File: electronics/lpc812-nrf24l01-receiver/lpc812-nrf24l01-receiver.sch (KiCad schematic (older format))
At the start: 10 parts, among them K1 CONN_3, K2 CONN_3, K3 CONN_3, K4 CONN_3, P1 CONN_4X2, U1 MCP1703T-3302E/CB, U2 LPC812M101JDH16_TSSOP16

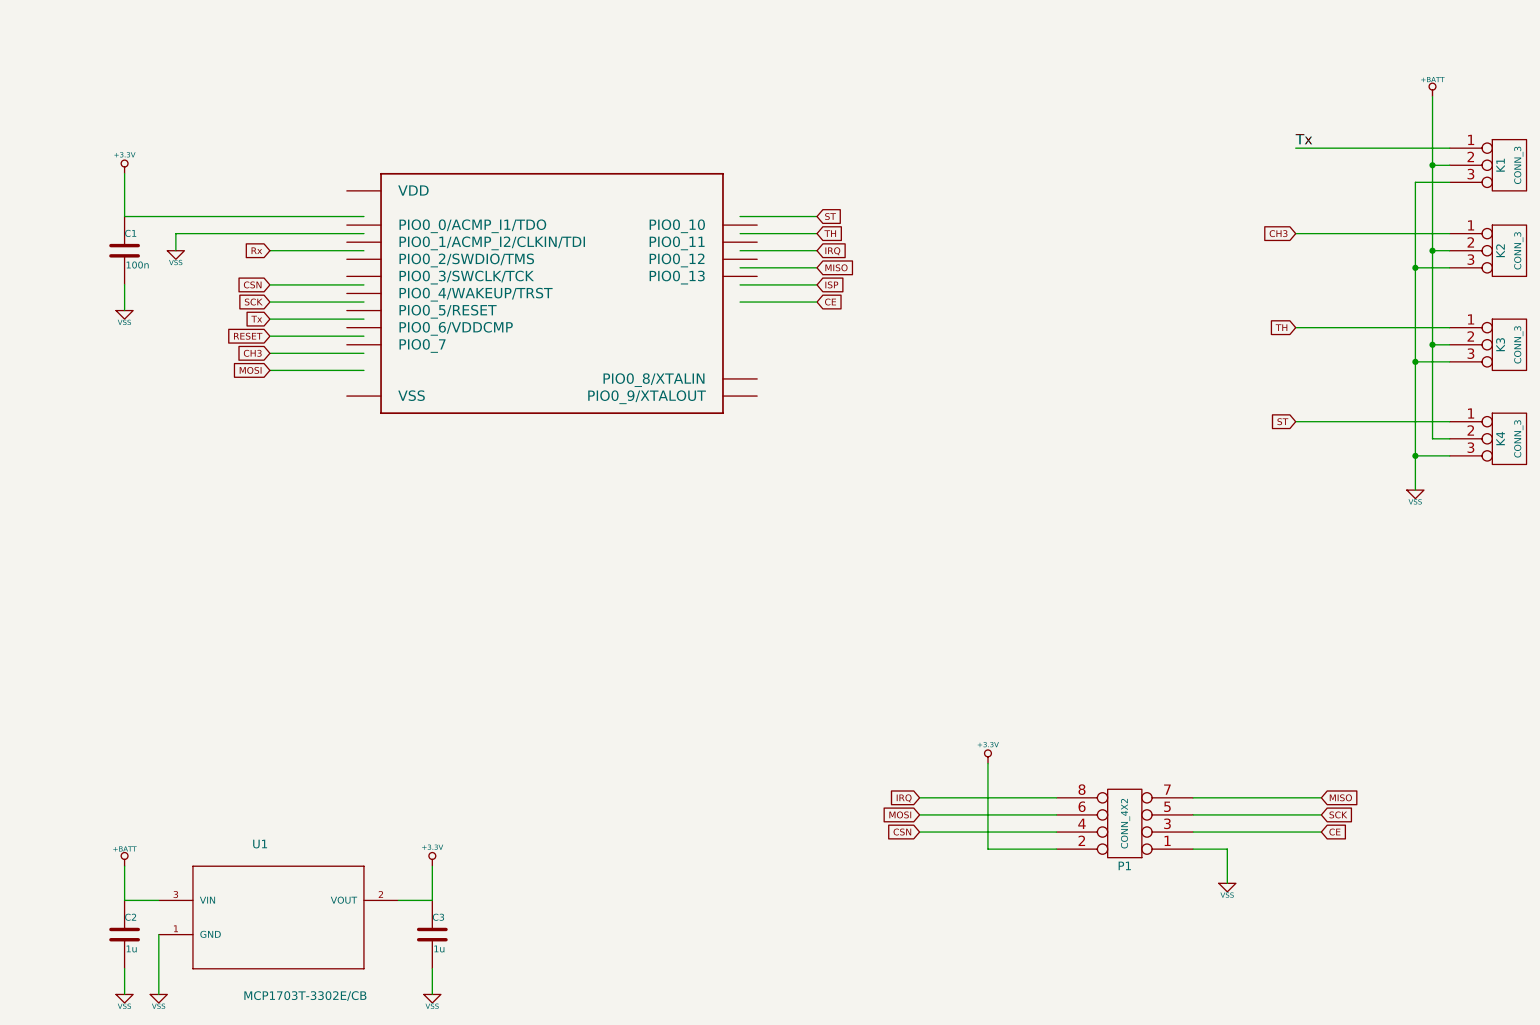
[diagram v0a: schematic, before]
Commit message: More tweaks to schematics and LPC812 symbol
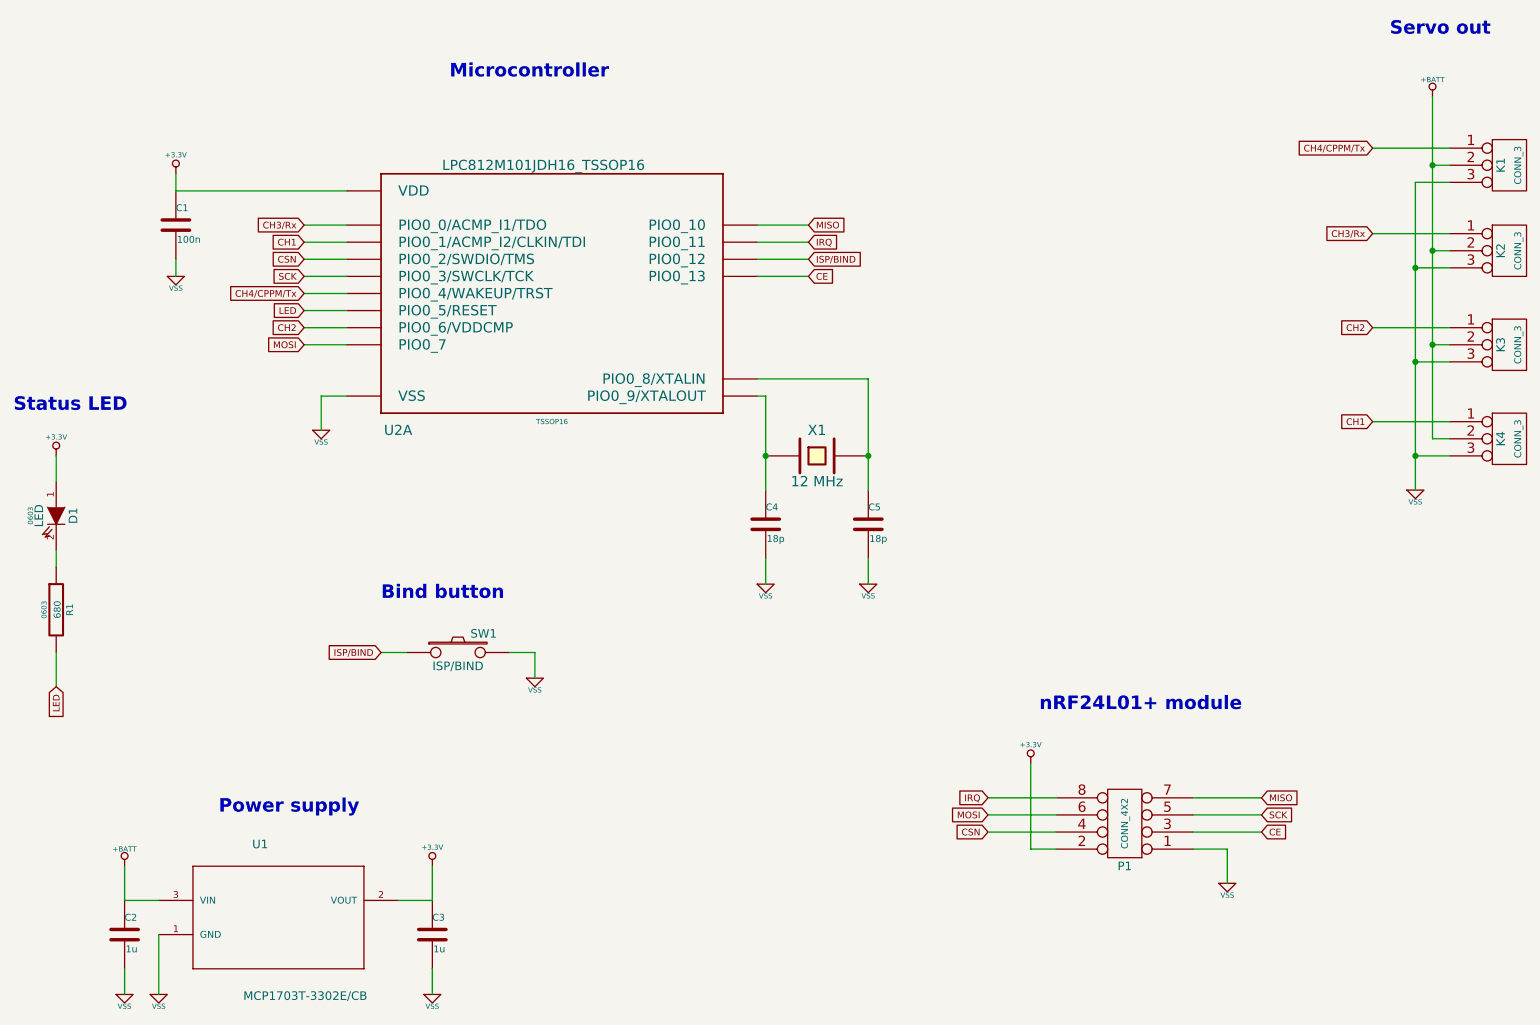
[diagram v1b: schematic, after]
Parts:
- added C4, C5: 18p, ~, symbol C
- added D1: LED, 0603, symbol LED
- added R1: 680, 0603, symbol R
- added SW1: ISP/BIND, ~, symbol SW_PUSH
- added X1: 12 MHz, ~, symbol CRYSTAL
- U2: footprint (none) -> TSSOP16
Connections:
- net labels added: CH1, CH2, CH3/Rx, CH4/CPPM/Tx, ISP/BIND, LED
- net labels removed: CH3, ISP, RESET, Rx, ST, TH, Tx
- wire segments 49 -> 68
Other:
- note added: "Bind button"
- note added: "Microcontroller"
- note added: "Power supply"
- note added: "Servo out"
- note added: "Status LED"
- note added: "nRF24L01+ module"
- moved on the sheet: C1

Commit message: Make ERC pass
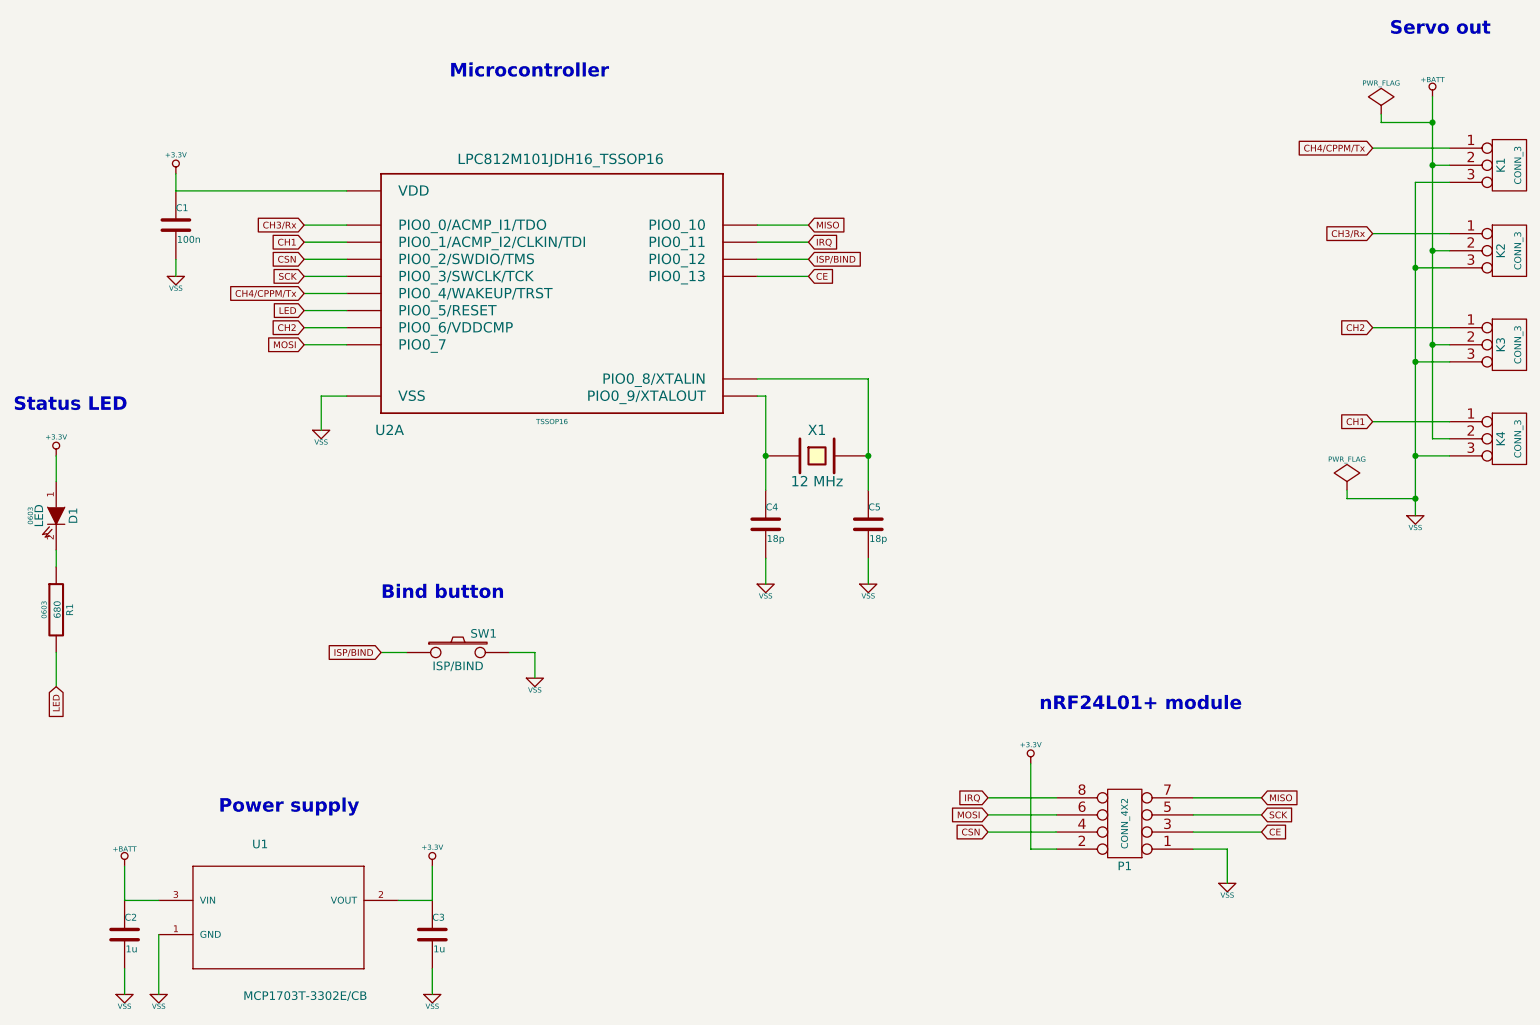
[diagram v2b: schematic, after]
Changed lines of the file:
@@
 L VSS #PWR010
 U 1 1 546EE412
-P 9650 3650
-F 0 "#PWR010" H 9650 3650 30  0001 C CNN
-F 1 "VSS" H 9650 3580 30  0000 C CNN
-F 2 "" H 9650 3650 60  0000 C CNN
-F 3 "" H 9650 3650 60  0000 C CNN
-	1    9650 3650
+P 9650 3800
+F 0 "#PWR010" H 9650 3800 30  0001 C CNN
+F 1 "VSS" H 9650 3730 30  0000 C CNN
+F 2 "" H 9650 3800 60  0000 C CNN
+F 3 "" H 9650 3800 60  0000 C CNN
+	1    9650 3800
 	1    0    0    -1
 $EndComp
@@
 U 1 1 546ED16B
 P 4600 2450
-F 0 "U2" H 3700 1600 59  0000 C CNN
-F 1 "LPC812M101JDH16_TSSOP16" H 4550 3150 59  0000 C CNN
+F 0 "U2" H 3650 1600 60  0000 C CNN
+F 1 "LPC812M101JDH16_TSSOP16" H 4650 3150 60  0000 C BNN
 F 2 "TSSOP16" H 4600 1650 30  0000 C CNN
 F 3 "" H 4600 2450 60  0000 C CNN
@@
 	9850 1850 9650 1850
 Wire Wire Line
-	9650 1850 9650 2350
-Wire Wire Line
-	9650 2350 9650 2900
-Wire Wire Line
-	9650 2900 9650 3450
-Wire Wire Line
-	9650 3450 9650 3650
+	9650 1850 9650 3800
 Wire Wire Line
 	9850 2350 9650 2350
@@
 	9750 3350 9850 3350
 Wire Wire Line
-	9750 1350 9750 1750
-Wire Wire Line
-	9750 1750 9750 2250
-Wire Wire Line
-	9750 2250 9750 2800
-Wire Wire Line
-	9750 2800 9750 3350
+	9750 1350 9750 3350
 Wire Wire Line
 	9750 1750 9850 1750
@@
 	3900 6600 3900 6450
 Wire Wire Line
-	5850 3100 5850 3450
-Wire Wire Line
-	5850 3450 5850 3650
+	5850 3100 5850 3650
 Connection ~ 5850 3450
 Wire Wire Line
-	6450 3000 6450 3450
-Wire Wire Line
-	6450 3450 6450 3650
+	6450 3000 6450 3650
 Connection ~ 6450 3450
 Wire Wire Line
@@
 Text Notes 2650 5550 0    79   ~ 16
 Power supply
+$Comp
+L PWR_FLAG #FLG017
+U 1 1 546F237F
+P 9450 1450
+F 0 "#FLG017" H 9450 1545 30  0001 C CNN
+F 1 "PWR_FLAG" H 9450 1630 30  0000 C CNN
+F 2 "" H 9450 1450 60  0000 C CNN
+F 3 "" H 9450 1450 60  0000 C CNN
+	1    9450 1450
+	1    0    0    -1
+$EndComp
+$Comp
+L PWR_FLAG #FLG018
+U 1 1 546F238E
+P 9250 3650
+F 0 "#FLG018" H 9250 3745 30  0001 C CNN
+F 1 "PWR_FLAG" H 9250 3830 30  0000 C CNN
+F 2 "" H 9250 3650 60  0000 C CNN
+F 3 "" H 9250 3650 60  0000 C CNN
+	1    9250 3650
+	1    0    0    -1
+$EndComp
+Wire Wire Line
+	9250 3650 9250 3700
+Wire Wire Line
+	9250 3700 9650 3700
+Connection ~ 9650 3700
+Wire Wire Line
+	9450 1450 9450 1500
+Wire Wire Line
+	9450 1500 9750 1500
+Connection ~ 9750 1500
 $EndSCHEMATC

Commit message: Update board
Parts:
- K1: value CONN_3 -> BAT
- K2: value CONN_3 -> CH3
- K3: value CONN_3 -> TH
- K4: value CONN_3 -> ST
- P1: value CONN_4X2 -> NRF24L01+
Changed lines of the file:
@@
 U 1 1 546ED329
 P 3000 6050
-F 0 "U1" H 2846 6349 50  0000 L BNN
-F 1 "MCP1703T-3302E/CB" H 2794 5462 50  0000 L BNN
+F 0 "U1" H 2500 5550 50  0000 L BNN
+F 1 "MCP1703T-3302E/CB" H 2550 6300 50  0000 L BNN
 F 2 "MCP1703-SOT95P300X145-3N" H 3000 6200 50  0001 C CNN
 F 3 "" H 3000 6050 60  0000 C CNN
@@
 P 7950 5600
 F 0 "P1" H 7950 5850 50  0000 C CNN
-F 1 "CONN_4X2" V 7950 5600 40  0000 C CNN
+F 1 "NRF24L01+" V 7950 5600 40  0000 C CNN
 F 2 "" H 7950 5600 60  0000 C CNN
 F 3 "" H 7950 5600 60  0000 C CNN
@@
 P 10200 1750
 F 0 "K1" V 10150 1750 50  0000 C CNN
-F 1 "CONN_3" V 10250 1750 40  0000 C CNN
+F 1 "BAT" V 10250 1750 40  0000 C CNN
 F 2 "" H 10200 1750 60  0000 C CNN
 F 3 "" H 10200 1750 60  0000 C CNN
@@
 P 10200 2250
 F 0 "K2" V 10150 2250 50  0000 C CNN
-F 1 "CONN_3" V 10250 2250 40  0000 C CNN
+F 1 "CH3" V 10250 2250 40  0000 C CNN
 F 2 "" H 10200 2250 60  0000 C CNN
 F 3 "" H 10200 2250 60  0000 C CNN
@@
 P 10200 2800
 F 0 "K3" V 10150 2800 50  0000 C CNN
-F 1 "CONN_3" V 10250 2800 40  0000 C CNN
+F 1 "TH" V 10250 2800 40  0000 C CNN
 F 2 "" H 10200 2800 60  0000 C CNN
 F 3 "" H 10200 2800 60  0000 C CNN
@@
 P 10200 3350
 F 0 "K4" V 10150 3350 50  0000 C CNN
-F 1 "CONN_3" V 10250 3350 40  0000 C CNN
+F 1 "ST" V 10250 3350 40  0000 C CNN
 F 2 "" H 10200 3350 60  0000 C CNN
 F 3 "" H 10200 3350 60  0000 C CNN
@@
 Wire Wire Line
 	8750 5650 8350 5650
-Text Notes 4000 1250 0    79   ~ 16
+Text Notes 4200 1450 0    79   ~ 16
 Microcontroller
 Text Notes 9500 1000 0    79   ~ 16

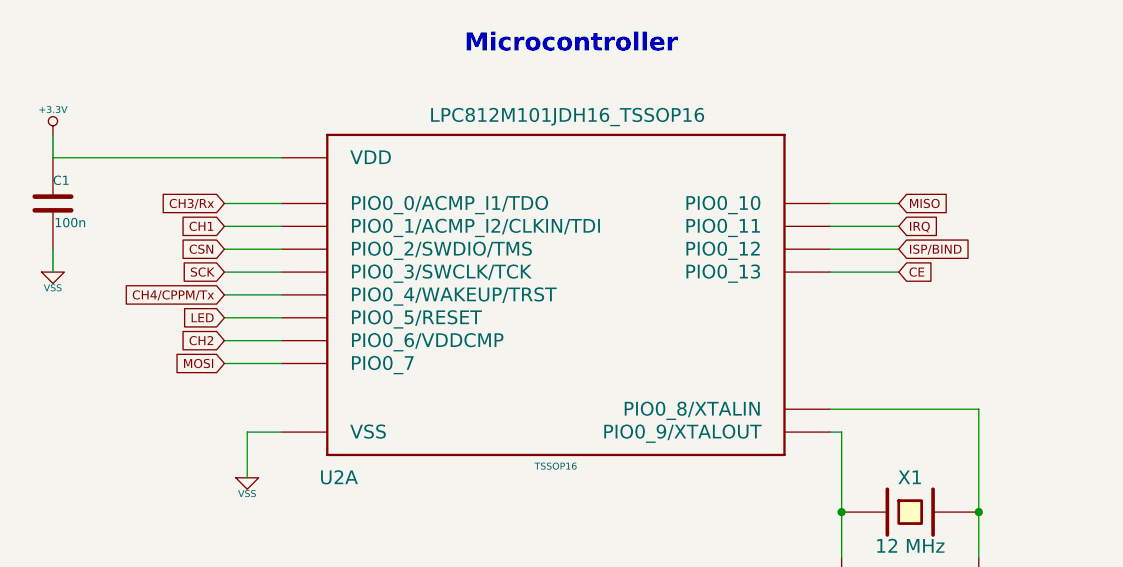
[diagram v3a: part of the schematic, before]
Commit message: Change pin-out for better layout
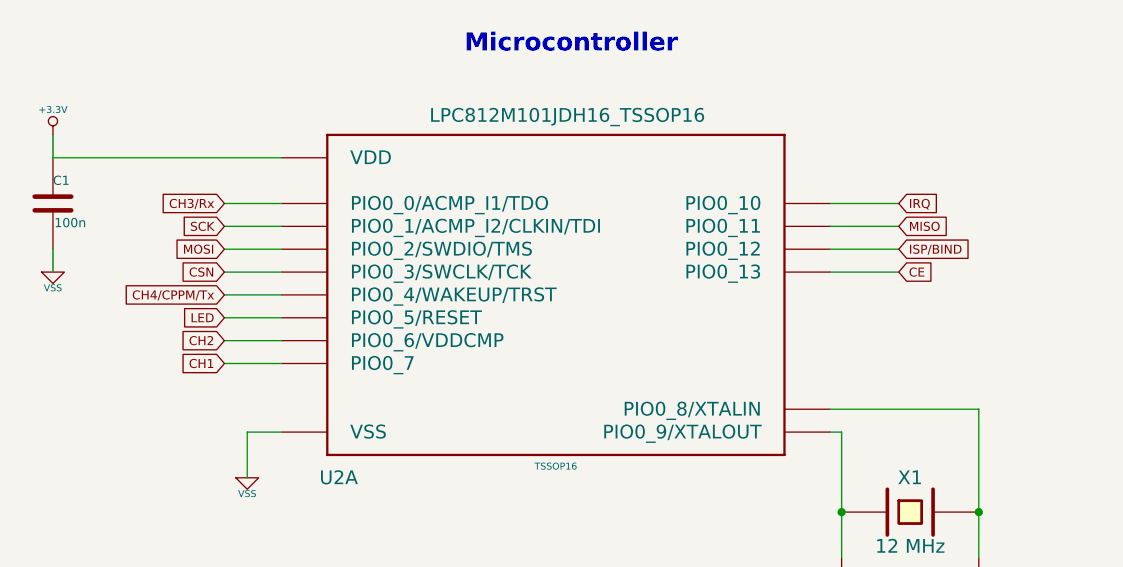
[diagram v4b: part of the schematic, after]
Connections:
- net CH1: now also U2.14 (PIO0_7); no longer U2.9 (PIO0_1/ACMP_I2/CLKIN/TDI)
- net CSN: now also U2.5 (PIO0_3/SWCLK/TCK); no longer U2.6 (PIO0_2/SWDIO/TMS)
- net IRQ: now also U2.8 (PIO0_10); no longer U2.7 (PIO0_11)
- net MISO: now also U2.7 (PIO0_11); no longer U2.8 (PIO0_10)
- net MOSI: now also U2.6 (PIO0_2/SWDIO/TMS); no longer U2.14 (PIO0_7)
- net SCK: now also U2.9 (PIO0_1/ACMP_I2/CLKIN/TDI); no longer U2.5 (PIO0_3/SWCLK/TCK)
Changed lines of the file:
@@
 Sheet 1 1
 Title ""
-Date "21 nov 2014"
+Date "22 nov 2014"
 Rev ""
 Comp ""
@@
 	1    0    0    -1
 $EndComp
-Text GLabel 6100 2100 2    39   Input ~ 0
+Text GLabel 6100 2200 2    39   Input ~ 0
 MISO
 Text GLabel 9400 2150 0    39   Input ~ 0
@@
 Text GLabel 6100 2400 2    39   Input ~ 0
 CE
-Text GLabel 6100 2200 2    39   Input ~ 0
+Text GLabel 6100 2100 2    39   Input ~ 0
 IRQ
 Text GLabel 3150 2100 0    39   Input ~ 0
 CH3/Rx
-Text GLabel 3150 2300 0    39   Input ~ 0
+Text GLabel 3150 2400 0    39   Input ~ 0
 CSN
-Text GLabel 3150 2400 0    39   Input ~ 0
+Text GLabel 3150 2200 0    39   Input ~ 0
 SCK
 Text GLabel 3150 2500 0    39   Input ~ 0
@@
 Text GLabel 3150 2600 0    39   Input ~ 0
 LED
-Text GLabel 3150 2800 0    39   Input ~ 0
+Text GLabel 3150 2300 0    39   Input ~ 0
 MOSI
 Text GLabel 3150 2700 0    39   Input ~ 0
@@
 	1    0    0    -1
 $EndComp
-Text GLabel 3150 2200 0    39   Input ~ 0
+Text GLabel 3150 2800 0    39   Input ~ 0
 CH1
 Text GLabel 9400 1650 0    39   Input ~ 0
